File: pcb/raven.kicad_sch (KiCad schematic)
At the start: 0 parts

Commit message: Add rough schematic layout
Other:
- added sheet MotorHub (motor-hub.kicad_sch)
- added sheet SensorHub (sensor-hub.kicad_sch)
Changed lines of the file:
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@@
 	(generator_version "8.0")
 	(paper "A4")
+	(sheet
+		(at 198.12 87.63)
+		(size 25.4 13.97)
+		(fields_autoplaced yes)
+		(stroke
+			(width 0.1524)
+			(type solid)
+		)
+		(fill
+			(color 0 0 0 0.0000)
+		)
+		(property "Sheetname" "SensorHub"
+			(at 198.12 86.9184 0)
+			(effects
+				(font
+					(size 1.27 1.27)
+				)
+				(justify left bottom)
+			)
+		)
+		(property "Sheetfile" "sensor-hub.kicad_sch"
+			(at 198.12 102.1846 0)
+			(effects
+				(font
+					(size 1.27 1.27)
+				)
+				(justify left top)
+			)
+		)
+		(instances
+			(project "raven"
+				(path "/38b0a34b-2047-47f6-90d7-ccdf77e8e212"
+					(page "19")
+				)
+			)
+		)
+	)
+	(sheet
+		(at 196.85 53.34)
+		(size 29.21 11.43)
+		(fields_autoplaced yes)
+		(stroke
+			(width 0.1524)
+			(type solid)
+		)
+		(fill
+			(color 0 0 0 0.0000)
+		)
+		(property "Sheetname" "MotorHub"
+			(at 196.85 52.6284 0)
+			(effects
+				(font
+					(size 1.27 1.27)
+				)
+				(justify left bottom)
+			)
+		)
+		(property "Sheetfile" "motor-hub.kicad_sch"
+			(at 196.85 65.3546 0)
+			(effects
+				(font
+					(size 1.27 1.27)
+				)
+				(justify left top)
+			)
+		)
+		(instances
+			(project "raven"
+				(path "/38b0a34b-2047-47f6-90d7-ccdf77e8e212"
+					(page "18")
+				)
+			)
+		)
+	)
 	(sheet_instances
 		(path "/"

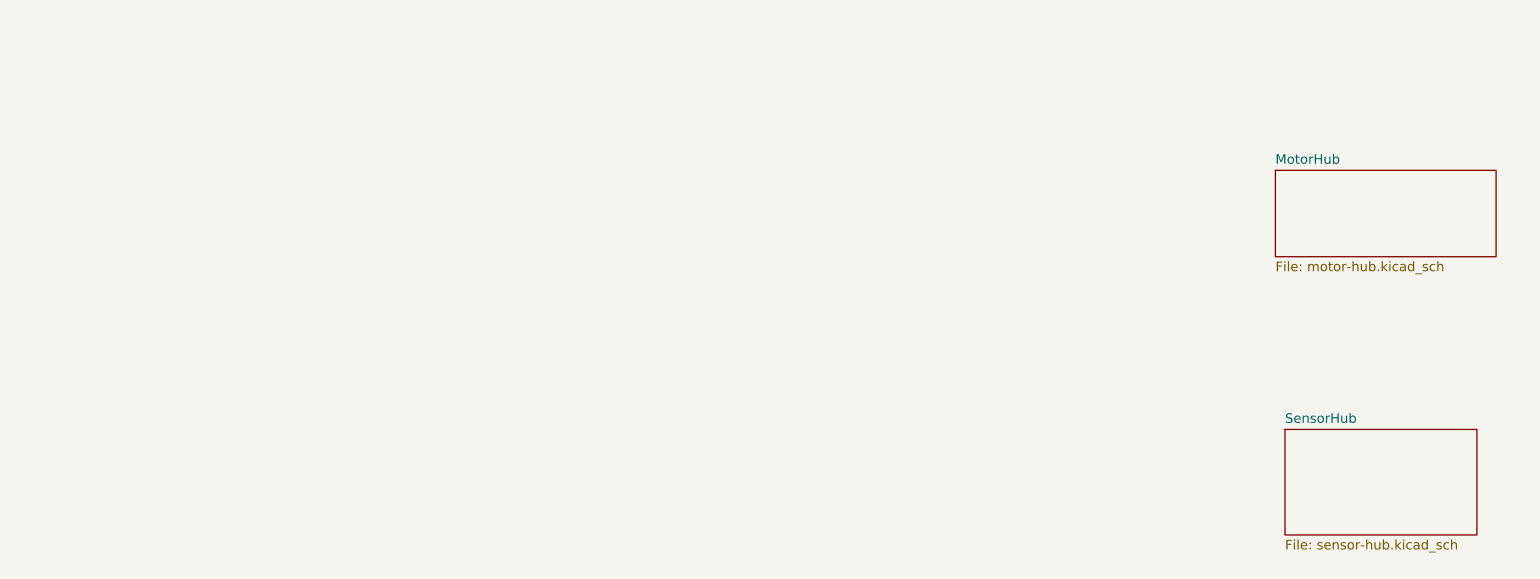
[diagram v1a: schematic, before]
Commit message: Remove sensor hub
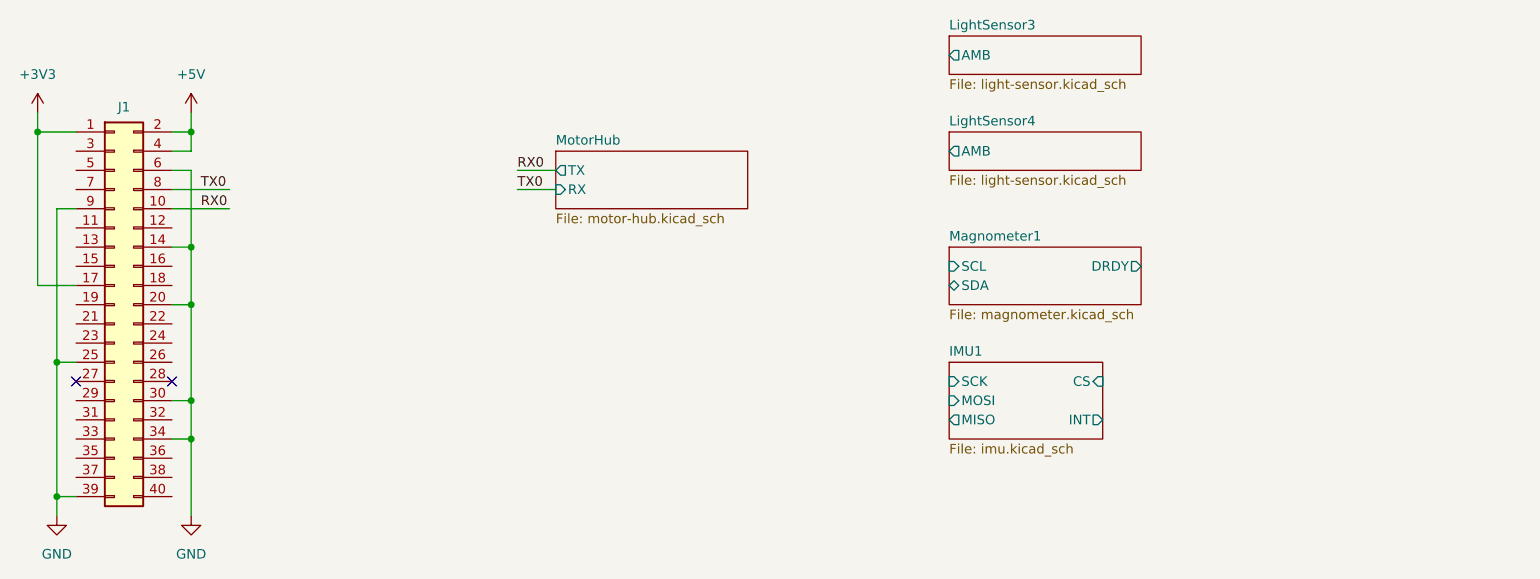
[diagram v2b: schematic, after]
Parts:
- added J1: Conn_02x20_Odd_Even, Connector_PinHeader_2.54mm:PinHeader_2x20_P2.54mm_Vertical, symbol Connector_Generic:Conn_02x20_Odd_Even
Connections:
- new net +3V3: J1.1 (Pin_1), J1.17 (Pin_17)
- new net +5V: J1.2 (Pin_2), J1.4 (Pin_4)
- new net GND: J1.14 (Pin_14), J1.20 (Pin_20), J1.25 (Pin_25), J1.30 (Pin_30), J1.34 (Pin_34), J1.39 (Pin_39), J1.6 (Pin_6), J1.9 (Pin_9)
- new net RX0: J1.10 (Pin_10)
- new net TX0: J1.8 (Pin_8)
- no-connect marks 0 -> 2
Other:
- removed sheet SensorHub
- added sheet IMU1 (imu.kicad_sch)
- added sheet LightSensor3 (light-sensor.kicad_sch)
- added sheet LightSensor4 (light-sensor.kicad_sch)
- added sheet Magnometer1 (magnometer.kicad_sch)
- sheet MotorHub ports: added RX, TX; removed none

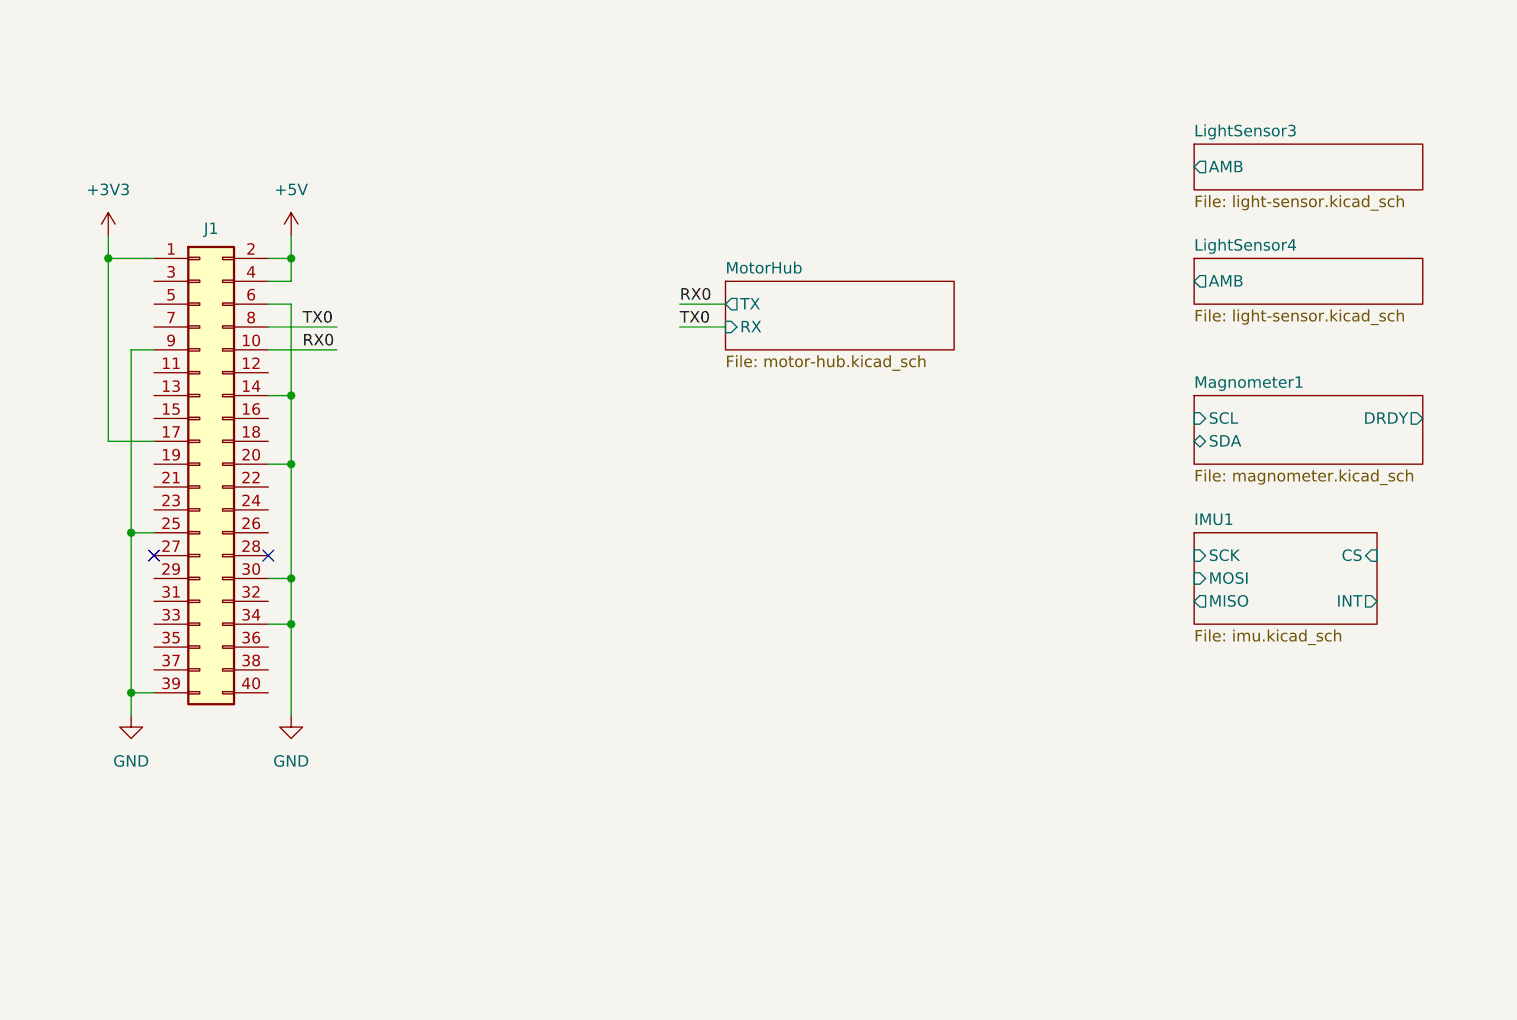
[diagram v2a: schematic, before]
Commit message: Finish schematic
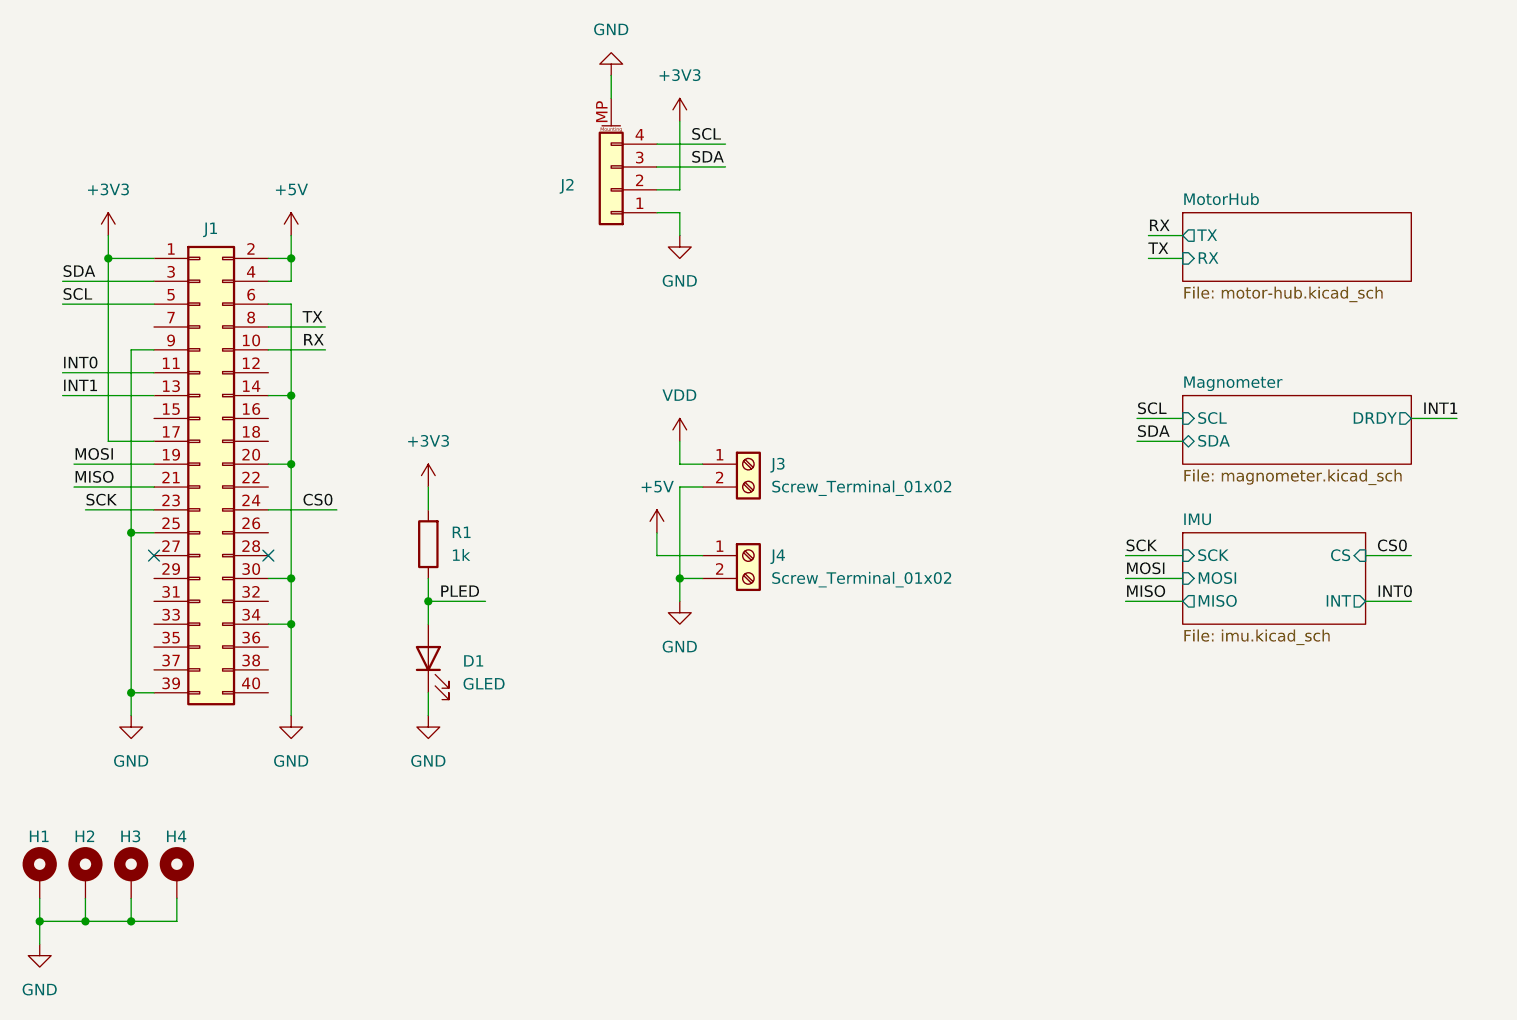
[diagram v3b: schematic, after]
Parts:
- added D1: GLED, LED_SMD:LED_0603_1608Metric, symbol Device:LED
- added H1, H2, H3, H4: MountingHole_Pad, MountingHole:MountingHole_2.5mm_Pad, symbol Mechanical:MountingHole_Pad
- added J2: Conn_01x04_MountingPin, Connector_JST:JST_SH_SM04B-SRSS-TB_1x04-1MP_P1.00mm_Horizontal, symbol Connector_Generic_MountingPin:Conn_01x04_MountingPin
- added J3, J4: Screw_Terminal_01x02, TerminalBlock_Phoenix:TerminalBlock_Phoenix_MKDS-1,5-2_1x02_P5.00mm_Horizontal, symbol Connector:Screw_Terminal_01x02
- added R1: 1k, Resistor_SMD:R_0402_1005Metric, symbol Device:R
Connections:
- net +3V3: now also J2.2 (Pin_2), R1.2
- net +5V: now also J4.1 (Pin_1)
- net GND: now also D1.1 (K), H1.1, H2.1, H3.1, H4.1, J2.1 (Pin_1), J2.MP (MountPin), J3.2 (Pin_2), J4.2 (Pin_2)
- net INT0: now reaches J1.11 (Pin_11)
- net INT1: now reaches J1.13 (Pin_13)
- net MOSI: now reaches J1.19 (Pin_19)
- net MISO: now reaches J1.21 (Pin_21)
- net SCK: now reaches J1.23 (Pin_23)
- net CS0: now reaches J1.24 (Pin_24)
- net SDA: now reaches J1.3 (Pin_3)
- net SDA: now also J2.3 (Pin_3)
- net SCL: now reaches J1.5 (Pin_5)
- net SCL: now also J2.4 (Pin_4)
- net RX0 renamed RX
- net TX0 renamed TX
- new net PLED: D1.2 (A), R1.1
- new net VDD: J3.1 (Pin_1)
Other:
- sheet IMU1 renamed IMU
- sheet Magnometer1 renamed Magnometer
- removed sheet LightSensor3
- removed sheet LightSensor4

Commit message: Save progress
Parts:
- J1: footprint Connector_PinHeader_2.54mm:PinHeader_2x20_P2.54mm_Vertical -> Connector_PinSocket_2.54mm:PinSocket_2x20_P2.54mm_Vertical
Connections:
- net INT0: now also J1.22 (Pin_22); no longer J1.11 (Pin_11)
- net INT1: now also J1.7 (Pin_7); no longer J1.13 (Pin_13)
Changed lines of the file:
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@@
+	)
+	(junction
+		(at 35.56 121.92)
+		(diameter 0)
+		(color 0 0 0 0)
 	)
 	(junction
@@
 		(color 0 0 0 0)
 	)
-	(junction
-		(at 35.56 121.92)
-		(diameter 0)
-		(color 0 0 0 0)
-	)
 	(no_connect
 		(at 38.1 81.28)
@@
 	(wire
 		(pts
+			(xy 40.64 119.38) (xy 40.64 121.92)
+		)
+		(stroke
+			(width 0)
+			(type default)
+		)
+	)
+	(wire
+		(pts
 			(xy 68.58 73.66) (xy 68.58 76.2)
 		)
@@
 	(wire
 		(pts
+			(xy 27.94 55.88) (xy 38.1 55.88)
+		)
+		(stroke
+			(width 0)
+			(type default)
+		)
+	)
+	(wire
+		(pts
 			(xy 93.98 35.56) (xy 101.6 35.56)
 		)
@@
 	(wire
 		(pts
+			(xy 50.8 73.66) (xy 58.42 73.66)
+		)
+		(stroke
+			(width 0)
+			(type default)
+		)
+	)
+	(wire
+		(pts
 			(xy 53.34 63.5) (xy 50.8 63.5)
 		)
@@
 	(wire
 		(pts
-			(xy 35.56 121.92) (xy 40.64 121.92)
-		)
-		(stroke
-			(width 0)
-			(type default)
-		)
-	)
-	(wire
-		(pts
 			(xy 33.02 45.72) (xy 33.02 48.26)
 		)
@@
 	(wire
 		(pts
-			(xy 27.94 63.5) (xy 38.1 63.5)
+			(xy 40.64 121.92) (xy 35.56 121.92)
 		)
 		(stroke
@@
 	(wire
 		(pts
-			(xy 27.94 60.96) (xy 38.1 60.96)
-		)
-		(stroke
-			(width 0)
-			(type default)
-		)
-	)
-	(wire
-		(pts
 			(xy 35.56 96.52) (xy 38.1 96.52)
 		)
@@
 		)
 	)
-	(wire
-		(pts
-			(xy 40.64 121.92) (xy 40.64 119.38)
-		)
-		(stroke
-			(width 0)
-			(type default)
-		)
-	)
-	(label "INT0"
-		(at 27.94 60.96 0)
+	(label "SDA"
+		(at 147.32 68.58 0)
 		(fields_autoplaced yes)
 		(effects
@@
 		)
 	)
-	(label "SDA"
-		(at 147.32 68.58 0)
+	(label "SCK"
+		(at 30.48 76.2 0)
 		(fields_autoplaced yes)
 		(effects
@@
 	)
 	(label "SCK"
-		(at 30.48 76.2 0)
+		(at 146.05 81.28 0)
 		(fields_autoplaced yes)
 		(effects
@@
 		)
 	)
-	(label "SCK"
-		(at 146.05 81.28 0)
+	(label "PLED"
+		(at 69.85 86.36 0)
 		(fields_autoplaced yes)
 		(effects
@@
 		)
 	)
-	(label "PLED"
-		(at 69.85 86.36 0)
+	(label "SDA"
+		(at 27.94 50.8 0)
 		(fields_autoplaced yes)
 		(effects
@@
 		)
 	)
-	(label "SDA"
-		(at 27.94 50.8 0)
+	(label "TX"
+		(at 148.59 48.26 0)
 		(fields_autoplaced yes)
 		(effects
@@
 		)
 	)
-	(label "TX"
-		(at 148.59 48.26 0)
+	(label "RX"
+		(at 148.59 45.72 0)
 		(fields_autoplaced yes)
 		(effects
@@
 		)
 	)
-	(label "INT1"
-		(at 27.94 63.5 0)
+	(label "MOSI"
+		(at 146.05 83.82 0)
 		(fields_autoplaced yes)
 		(effects
@@
 		)
 	)
-	(label "RX"
-		(at 148.59 45.72 0)
+	(label "SDA"
+		(at 97.79 38.1 0)
 		(fields_autoplaced yes)
 		(effects
@@
 		)
 	)
-	(label "MOSI"
-		(at 146.05 83.82 0)
+	(label "MISO"
+		(at 146.05 86.36 0)
 		(fields_autoplaced yes)
 		(effects
@@
 		)
 	)
-	(label "SDA"
-		(at 97.79 38.1 0)
+	(label "RX"
+		(at 54.61 58.42 0)
 		(fields_autoplaced yes)
 		(effects
@@
 		)
 	)
-	(label "MISO"
-		(at 146.05 86.36 0)
+	(label "CS0"
+		(at 173.99 81.28 0)
 		(fields_autoplaced yes)
 		(effects
@@
 		)
 	)
-	(label "RX"
-		(at 54.61 58.42 0)
+	(label "SCL"
+		(at 97.79 35.56 0)
 		(fields_autoplaced yes)
 		(effects
@@
 		)
 	)
-	(label "CS0"
-		(at 173.99 81.28 0)
+	(label "TX"
+		(at 54.61 55.88 0)
 		(fields_autoplaced yes)
 		(effects
@@
 		)
 	)
-	(label "SCL"
-		(at 97.79 35.56 0)
+	(label "MOSI"
+		(at 29.21 71.12 0)
 		(fields_autoplaced yes)
 		(effects
@@
 		)
 	)
-	(label "TX"
-		(at 54.61 55.88 0)
+	(label "SCL"
+		(at 27.94 53.34 0)
 		(fields_autoplaced yes)
 		(effects
@@
 		)
 	)
-	(label "MOSI"
-		(at 29.21 71.12 0)
+	(label "INT1"
+		(at 179.07 66.04 0)
 		(fields_autoplaced yes)
 		(effects
@@
 		)
 	)
-	(label "SCL"
-		(at 27.94 53.34 0)
+	(label "INT1"
+		(at 27.94 55.88 0)
 		(fields_autoplaced yes)
 		(effects
@@
 		)
 	)
-	(label "INT1"
-		(at 179.07 66.04 0)
+	(label "MISO"
+		(at 29.21 73.66 0)
 		(fields_autoplaced yes)
 		(effects
@@
 		)
 	)
-	(label "MISO"
-		(at 29.21 73.66 0)
+	(label "CS0"
+		(at 54.61 76.2 0)
 		(fields_autoplaced yes)
 		(effects
@@
 		)
 	)
-	(label "CS0"
-		(at 54.61 76.2 0)
+	(label "INT0"
+		(at 54.61 73.66 0)
 		(fields_autoplaced yes)
 		(effects
@@
 	)
 	(symbol
-		(lib_id "Mechanical:MountingHole_Pad")
-		(at 40.64 116.84 0)
-		(unit 1)
-		(exclude_from_sim yes)
-		(in_bom no)
-		(on_board yes)
-		(dnp no)
-		(property "Reference" "H4"
-			(at 39.37 112.522 0)
-			(effects
-				(font
-					(size 1.27 1.27)
-				)
-				(justify left)
-			)
-		)
-		(property "Value" "MountingHole_Pad"
-			(at 43.18 116.8399 0)
-			(effects
-				(font
-					(size 1.27 1.27)
-				)
-				(justify left)
-				(hide yes)
-			)
-		)
-		(property "Footprint" "MountingHole:MountingHole_2.5mm_Pad"
-			(at 40.64 116.84 0)
-			(effects
-				(font
-					(size 1.27 1.27)
-				)
-				(hide yes)
-			)
-		)
-		(property "Datasheet" "~"
-			(at 40.64 116.84 0)
-			(effects
-				(font
-					(size 1.27 1.27)
-				)
-				(hide yes)
-			)
-		)
-		(property "Description" "Mounting Hole with connection"
-			(at 40.64 116.84 0)
-			(effects
-				(font
-					(size 1.27 1.27)
-				)
-				(hide yes)
-			)
-		)
-		(pin "1"
-		)
-		(instances
-			(project "raven"
-				(path "/38b0a34b-2047-47f6-90d7-ccdf77e8e212"
-					(reference "H4")
-					(unit 1)
-				)
-			)
-		)
-	)
-	(symbol
 		(lib_id "power:VDD")
 		(at 96.52 68.58 0)
@@
 	)
 	(symbol
+		(lib_id "Mechanical:MountingHole_Pad")
+		(at 40.64 116.84 0)
+		(unit 1)
+		(exclude_from_sim yes)
+		(in_bom no)
+		(on_board yes)
+		(dnp no)
+		(property "Reference" "H4"
+			(at 39.37 112.522 0)
+			(effects
+				(font
+					(size 1.27 1.27)
+				)
+				(justify left)
+			)
+		)
+		(property "Value" "MountingHole_Pad"
+			(at 43.18 116.8399 0)
+			(effects
+				(font
+					(size 1.27 1.27)
+				)
+				(justify left)
+				(hide yes)
+			)
+		)
+		(property "Footprint" "MountingHole:MountingHole_2.5mm_Pad"
+			(at 40.64 116.84 0)
+			(effects
+				(font
+					(size 1.27 1.27)
+				)
+				(hide yes)
+			)
+		)
+		(property "Datasheet" "~"
+			(at 40.64 116.84 0)
+			(effects
+				(font
+					(size 1.27 1.27)
+				)
+				(hide yes)
+			)
+		)
+		(property "Description" "Mounting Hole with connection"
+			(at 40.64 116.84 0)
+			(effects
+				(font
+					(size 1.27 1.27)
+				)
+				(hide yes)
+			)
+		)
+		(pin "1"
+		)
+		(instances
+			(project "raven"
+				(path "/38b0a34b-2047-47f6-90d7-ccdf77e8e212"
+					(reference "H4")
+					(unit 1)
+				)
+			)
+		)
+	)
+	(symbol
 		(lib_id "power:GND")
 		(at 96.52 86.36 0)
@@
 			)
 		)
-		(property "Footprint" "Connector_PinHeader_2.54mm:PinHeader_2x20_P2.54mm_Vertical"
+		(property "Footprint" "Connector_PinSocket_2.54mm:PinSocket_2x20_P2.54mm_Vertical"
 			(at 43.18 71.12 0)
 			(effects
